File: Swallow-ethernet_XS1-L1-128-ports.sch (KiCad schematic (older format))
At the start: 13 parts, among them U11 XS1-L1-128

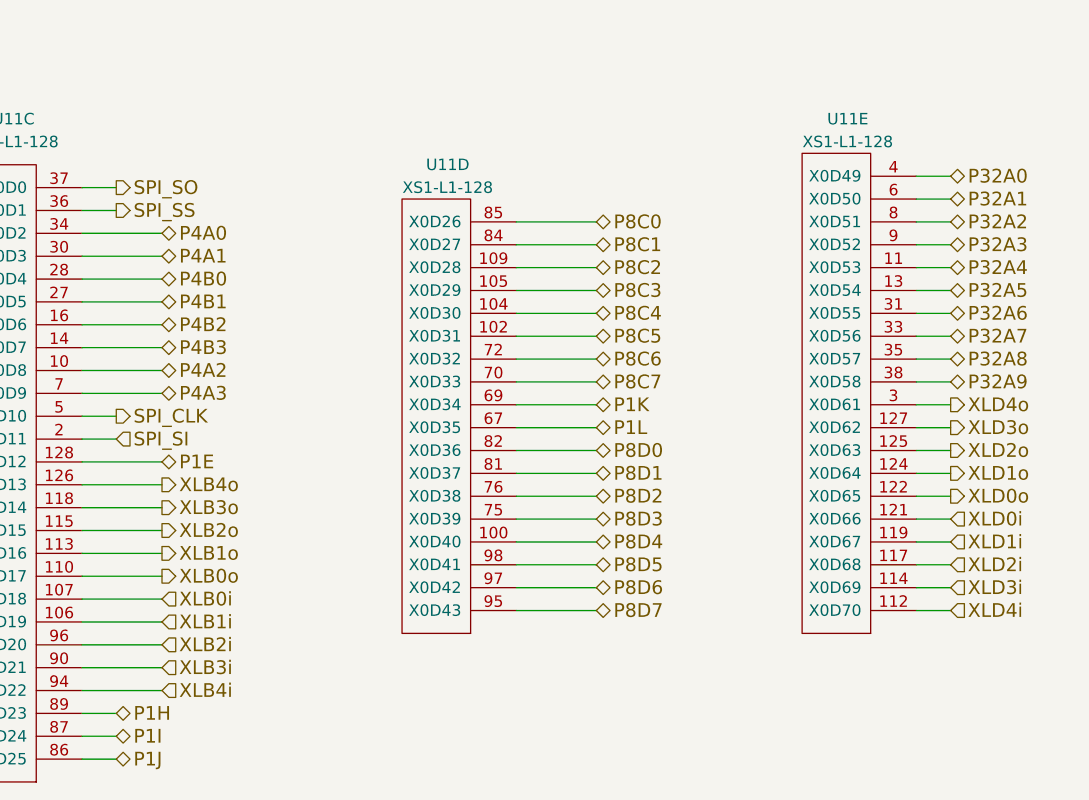
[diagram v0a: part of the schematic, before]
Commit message: Created pinout for SDRAM + ethernet I/O board. Pushed pinout to schematic.
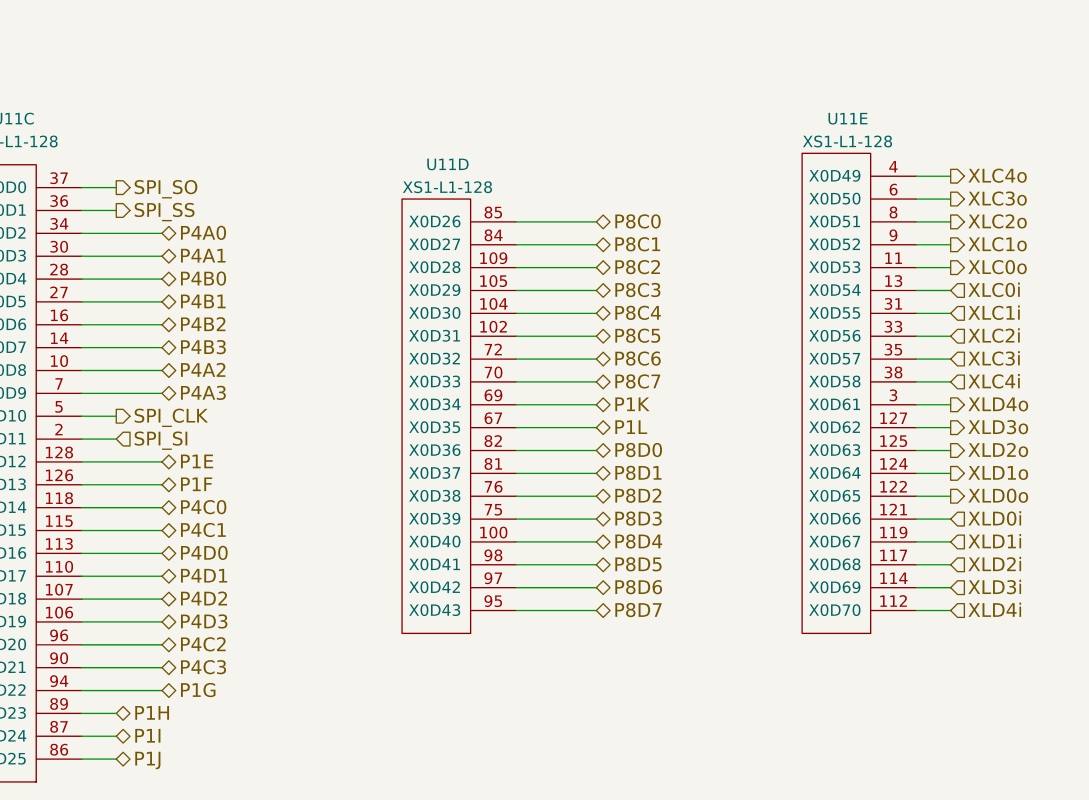
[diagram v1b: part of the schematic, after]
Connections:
- net P32A0 renamed XLC4o
- net P32A1 renamed XLC3o
- net P32A2 renamed XLC2o
- net P32A3 renamed XLC1o
- net P32A4 renamed XLC0o
- net P32A5 renamed XLC0i
- net P32A6 renamed XLC1i
- net P32A7 renamed XLC2i
- net P32A8 renamed XLC3i
- net P32A9 renamed XLC4i
- net XLB0i renamed P4D2
- net XLB0o renamed P4D1
- net XLB1i renamed P4D3
- net XLB1o renamed P4D0
- net XLB2i renamed P4C2
- net XLB2o renamed P4C1
- net XLB3i renamed P4C3
- net XLB3o renamed P4C0
- net XLB4i renamed P1G
- net XLB4o renamed P1F
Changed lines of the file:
@@
-EESchema Schematic File Version 2  date 29/09/2012 20:57:41
+EESchema Schematic File Version 2  date 30/09/2012 20:10:31
 LIBS:power
 LIBS:device
@@
 Sheet 3 4
 Title ""
-Date "29 sep 2012"
+Date "30 sep 2012"
 Rev ""
 Comp ""
@@
 Comment4 ""
 $EndDescr
+Text HLabel 4650 6250 2    60   BiDi ~ 0
+P1F
+Text HLabel 4650 7150 2    60   BiDi ~ 0
+P1G
+Text HLabel 4650 7050 2    60   BiDi ~ 0
+P4C3
+Text HLabel 4650 6950 2    60   BiDi ~ 0
+P4C2
+Text HLabel 4650 6850 2    60   BiDi ~ 0
+P4D3
+Text HLabel 4650 6750 2    60   BiDi ~ 0
+P4D2
+Text HLabel 4650 6650 2    60   BiDi ~ 0
+P4D1
+Text HLabel 4650 6550 2    60   BiDi ~ 0
+P4D0
+Text HLabel 4650 6450 2    60   BiDi ~ 0
+P4C1
+Text HLabel 4650 6350 2    60   BiDi ~ 0
+P4C0
 Connection ~ 2800 3850
 Wire Wire Line
@@
 Text HLabel 4650 5450 2    60   BiDi ~ 0
 P4B1
-Text HLabel 4650 7150 2    60   Input ~ 0
-XLB4i
-Text HLabel 4650 6250 2    60   Output ~ 0
-XLB4o
-Text HLabel 4650 6350 2    60   Output ~ 0
-XLB3o
 Text HLabel 4650 5150 2    60   BiDi ~ 0
 P4A0
@@
 Text HLabel 8100 5900 2    60   Output ~ 0
 XLD4o
-Text HLabel 8100 5800 2    60   BiDi ~ 0
-P32A9
-Text HLabel 8100 5700 2    60   BiDi ~ 0
-P32A8
-Text HLabel 8100 5600 2    60   BiDi ~ 0
-P32A7
-Text HLabel 8100 5500 2    60   BiDi ~ 0
-P32A6
-Text HLabel 8100 5400 2    60   BiDi ~ 0
-P32A5
-Text HLabel 8100 5300 2    60   BiDi ~ 0
-P32A4
-Text HLabel 8100 5200 2    60   BiDi ~ 0
-P32A3
-Text HLabel 8100 5100 2    60   BiDi ~ 0
-P32A2
-Text HLabel 8100 5000 2    60   BiDi ~ 0
-P32A1
-Text HLabel 8100 4900 2    60   BiDi ~ 0
-P32A0
+Text HLabel 8100 5800 2    60   Input ~ 0
+XLC4i
+Text HLabel 8100 5700 2    60   Input ~ 0
+XLC3i
+Text HLabel 8100 5600 2    60   Input ~ 0
+XLC2i
+Text HLabel 8100 5500 2    60   Input ~ 0
+XLC1i
+Text HLabel 8100 5400 2    60   Input ~ 0
+XLC0i
+Text HLabel 8100 5300 2    60   Output ~ 0
+XLC0o
+Text HLabel 8100 5200 2    60   Output ~ 0
+XLC1o
+Text HLabel 8100 5100 2    60   Output ~ 0
+XLC2o
+Text HLabel 8100 5000 2    60   Output ~ 0
+XLC3o
+Text HLabel 8100 4900 2    60   Output ~ 0
+XLC4o
 Text HLabel 4650 5250 2    60   BiDi ~ 0
 P4A1
@@
 Text HLabel 6550 5500 2    60   BiDi ~ 0
 P8C4
-Text HLabel 4650 6750 2    60   Input ~ 0
-XLB0i
-Text HLabel 4650 6850 2    60   Input ~ 0
-XLB1i
-Text HLabel 4650 6950 2    60   Input ~ 0
-XLB2i
-Text HLabel 4650 7050 2    60   Input ~ 0
-XLB3i
-Text HLabel 4650 6650 2    60   Output ~ 0
-XLB0o
-Text HLabel 4650 6550 2    60   Output ~ 0
-XLB1o
-Text HLabel 4650 6450 2    60   Output ~ 0
-XLB2o
 $Comp
 L GND #PWR082
